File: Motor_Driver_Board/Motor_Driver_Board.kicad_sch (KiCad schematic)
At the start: 5 parts, among them J1 Conn_01x02_MountingPin, J2 Conn_01x04_MountingPin

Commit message: Shcematic and layout
Updated the schematic.
Updated the layout.
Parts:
- removed J1: Conn_01x02_MountingPin, Connector_PinHeader_2.54mm:PinHeader_1x02_P2.54mm_Vertical, symbol Connector_Generic_MountingPin:Conn_01x02_MountingPin
- removed J2: Conn_01x04_MountingPin, Connector_PinHeader_2.54mm:PinHeader_1x04_P2.54mm_Horizontal, symbol Connector_Generic_MountingPin:Conn_01x04_MountingPin
- added C2: 100u, Capacitor_THT:CP_Radial_D6.3mm_P2.50mm, symbol Device:C_Polarized
- added C3: 10u, Capacitor_SMD:C_1206_3216Metric, symbol Device:C
- added C4, C5, C6: 47u, Capacitor_SMD:C_1206_3216Metric, symbol Device:C
- added C7, C8, C9: 10n, Capacitor_SMD:C_0603_1608Metric, symbol Device:C
- added D1: SS34, Diode_SMD:D_SMA, symbol Diode:SS34
- added H1, H2, H3, H4: MH, MountingHole:MountingHole_3.2mm_M3, symbol Mechanical:MountingHole
- added J1: POWER, Connector_PinHeader_2.54mm:PinHeader_1x02_P2.54mm_Vertical, symbol Connector_Generic:Conn_01x02
- added J2: MOTOR, Connector_PinHeader_2.54mm:PinHeader_1x04_P2.54mm_Vertical, symbol Connector_Generic:Conn_01x04
- added J3: LCD, Connector_PinHeader_2.54mm:PinHeader_1x04_P2.54mm_Vertical, symbol Connector_Generic:Conn_01x04
- added L1: FXL1040-680-M, Inductor_SMD:L_Sunlord_MWSA1005S, symbol Device:L
- added R1, R10, R11, R2, R3, R4, R5, R6, R7, R8, R9: 10K, Resistor_SMD:R_0603_1608Metric, symbol Device:R
- added SW1: ENCODER, Rotary_Encoder:RotaryEncoder_Alps_EC11E-Switch_Vertical_H20mm_CircularMountingHoles, symbol Device:RotaryEncoder_Switch_MP
- added U1: XL1509-5.0, Package_SO:SOIC-8_3.9x4.9mm_P1.27mm, symbol Regulator_Switching:XL1509-5.0
- A1: value Pololu_Breakout_A4988 -> A4988
- C1: value C_Polarized 100uF -> 100u; footprint Capacitor_THT:CP_Axial_L18.0mm_D8.0mm_P25.00mm_Horizontal -> Capacitor_THT:CP_Radial_D6.3mm_P2.50mm
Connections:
- net GND: now also C2.2, C3.2, C4.2, C5.2, C6.2, C7.2, C8.2, C9.2, D1.2 (A), J1.2 (Pin_2), J3.4 (Pin_4), R7.2, R8.2, R9.2, SW1.C, SW1.S2, U1.5 (GND), U1.6 (GND), U1.7 (GND), U1.8 (GND); no longer A2.33 (AGND)
- net MS1: now reaches A1.10 (MS1), A2.6 (GPIO4)
- net MS1: now also R7.1
- net MS2: now reaches A1.11 (MS2), A2.5 (GPIO3)
- net MS2: now also R8.1
- net MS3: now reaches A1.12 (MS3), A2.4 (GPIO2)
- net MS3: now also R9.1
- net RST: now reaches A1.13 (~{RESET}), A1.14 (~{SLEEP})
- net DIR: now reaches A1.15 (STEP), A2.2 (GPIO1)
- net STEP: now reaches A1.16 (DIR), A2.1 (GPIO0)
- net at A2.40 (VBUS): no longer A1.2 (VDD)
- net B1: now reaches A1.3 (1B)
- net B1: now also J2.1 (Pin_1)
- net A1: now reaches A1.4 (1A)
- net A1: now also J2.2 (Pin_2)
- net A2: now reaches A1.5 (2A)
- net A2: now also J2.4 (Pin_4)
- net B2: now reaches A1.6 (2B)
- net B2: now also J2.3 (Pin_3)
- net VCC: now reaches A1.8 (VMOT), C1.1
- net VCC: now also C2.1, C3.1, J1.1 (Pin_1), U1.1 (VIN), U1.4 (~{EN})
- net SDA: now reaches A2.11 (GPIO8)
- net SDA: now also J3.1 (Pin_1), R10.2
- net SCL: now reaches A2.12 (GPIO9)
- net SCL: now also J3.2 (Pin_2), R11.2
- net ENC_CW: now reaches A2.15 (GPIO11)
- net ENC_CW: now also C7.1, R6.2
- net ENC_CC: now reaches A2.17 (GPIO13)
- net ENC_CC: now also C8.1, R4.2
- net ENC_SW: now reaches A2.20 (GPIO15)
- net ENC_SW: now also C9.1, R5.1
- net +3V3: now reaches A2.36 (3V3)
- net +3V3: now also J3.3 (Pin_3), R1.1, R10.1, R11.1, R2.1, R3.1
- net +5V: now reaches A2.39 (VSYS)
- net +5V: now also A1.2 (VDD), C4.1, C5.1, C6.1, L1.2, U1.3 (FB)
- new net: R2.2, R4.1, SW1.A
- new net: R1.2, R6.1, SW1.B
- new net: R3.2, R5.2, SW1.S1
- new net DC_OUT: D1.1 (K), L1.1, U1.2 (OUT)
- no-connect marks 29 -> 25
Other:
- note added: "DC-DC Regulator 5V/2A"
- note added: "ENCODER"
- note added: "I2C LCD"
- note added: "Motor"
- note added: "Power In 8-35V"
- note added: "RP PICO / RP2040"
- note removed: "Motor Input"
- note removed: "Motor Input Power 8-35V"
- moved on the sheet: A1, A2, C1

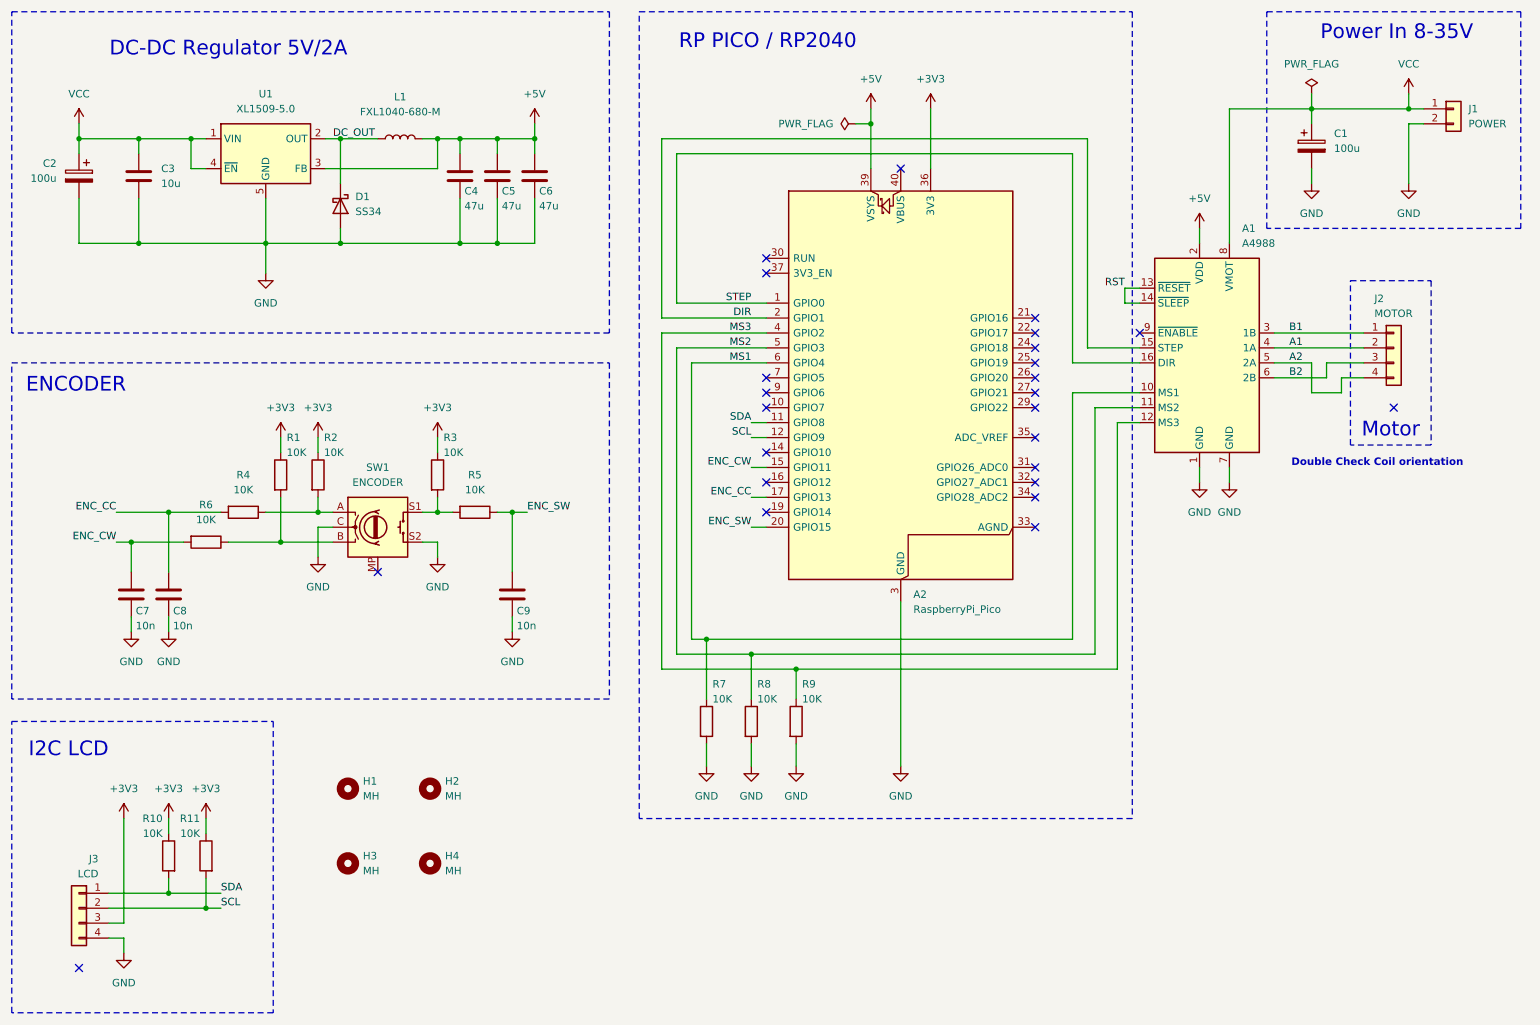
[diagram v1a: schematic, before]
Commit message: Switch to RP2040-Zero
Switched controller to RP2040-Zero to save space, schematic updated.
PCB layout in progress
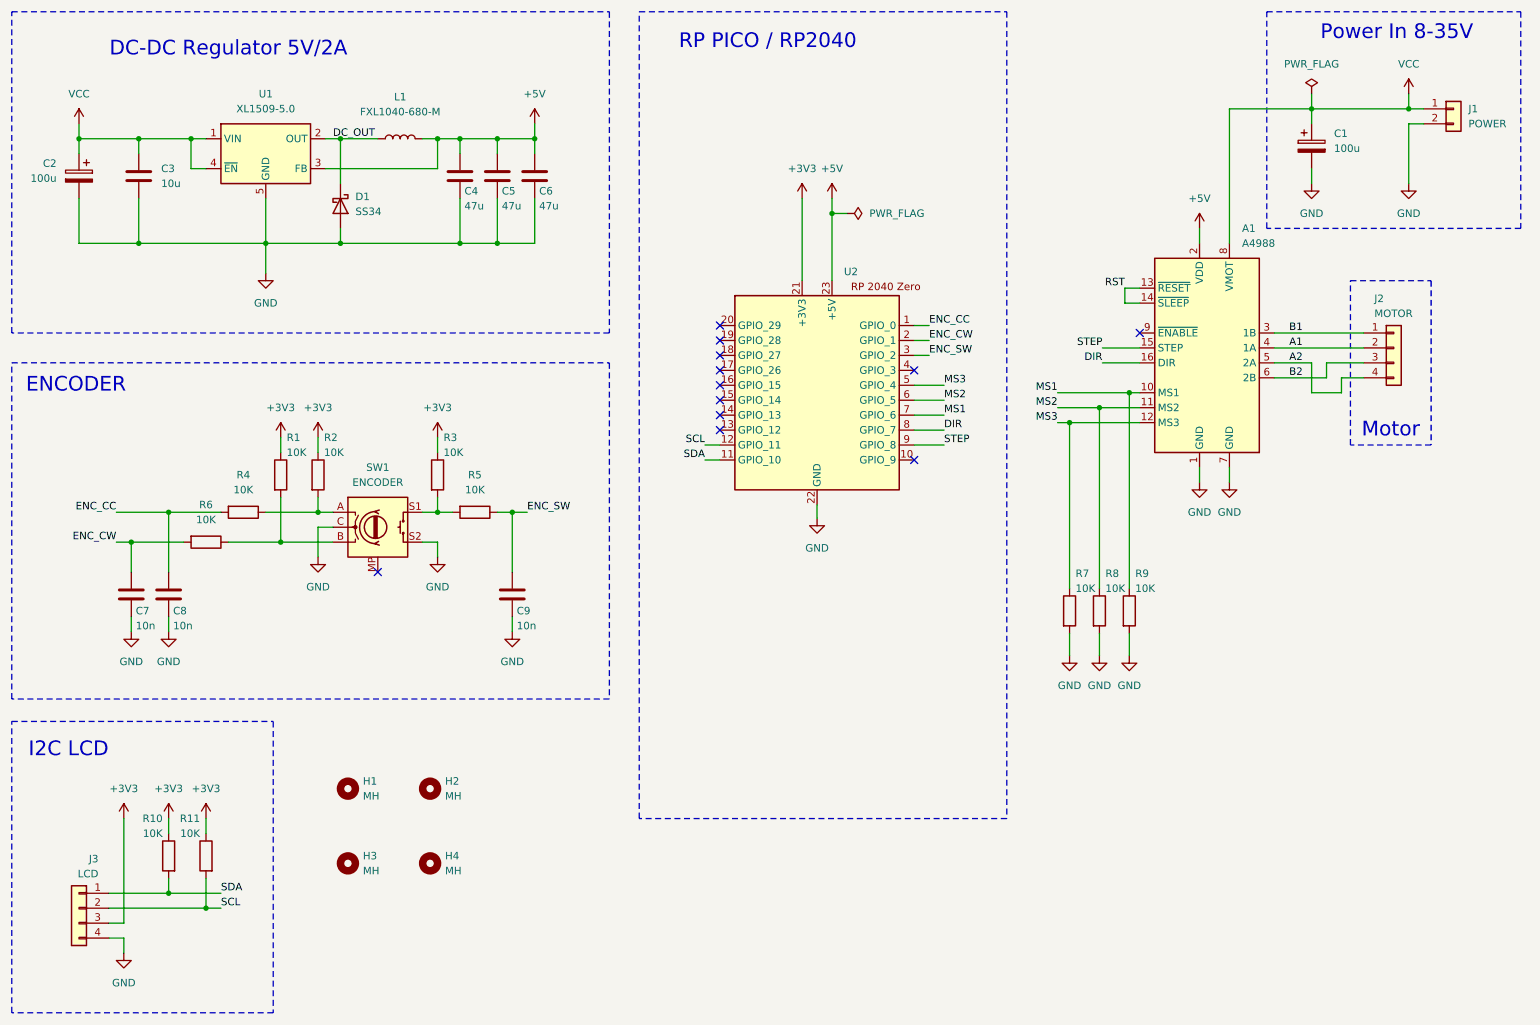
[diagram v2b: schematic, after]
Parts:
- removed A2: RaspberryPi_Pico, Module:RaspberryPi_Pico_Common_Unspecified, symbol MCU_Module:RaspberryPi_Pico
- added U2: (no value), RP2040Zero:MODULE_RP2040-ZERO, symbol RP2040_Zero:RP2040_Zero
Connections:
- net +3V3: now also U2.21 (+3V3)
- net +5V: now also U2.23 (+5V)
- net DIR: now also A1.16 (DIR), U2.8 (GPIO_7); no longer A1.15 (STEP)
- net ENC_CC: now also U2.1 (GPIO_0)
- net ENC_CW: now also U2.2 (GPIO_1)
- net ENC_SW: now also U2.3 (GPIO_2)
- net GND: now also U2.22 (GND)
- net MS1: now also R9.1, U2.7 (GPIO_6); no longer R7.1
- net MS2: now also U2.6 (GPIO_5)
- net MS3: now also R7.1, U2.5 (GPIO_4); no longer R9.1
- net SCL: now also U2.12 (GPIO_11)
- net SDA: now also U2.11 (GPIO_10)
- net STEP: now also A1.15 (STEP), U2.9 (GPIO_8); no longer A1.16 (DIR)
- no-connect marks 25 -> 12
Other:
- note removed: "Double Check Coil orientation"
- moved on the sheet: R7, R8, R9

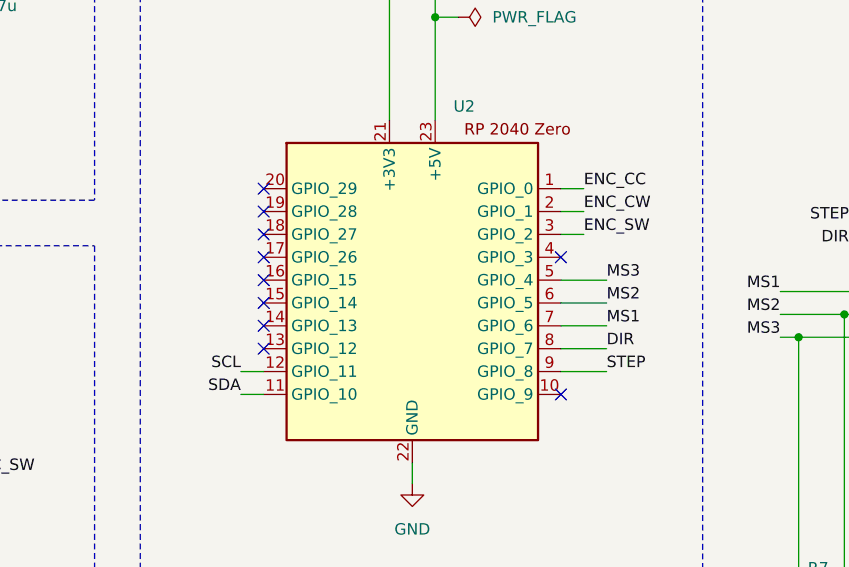
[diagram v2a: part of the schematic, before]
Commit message: Added RP2040-Zero Microcontroller
Switched previous Pi Pico to RP2040-Zero by Waveshare to reduce overall board size. Layout complete, via hatching still required
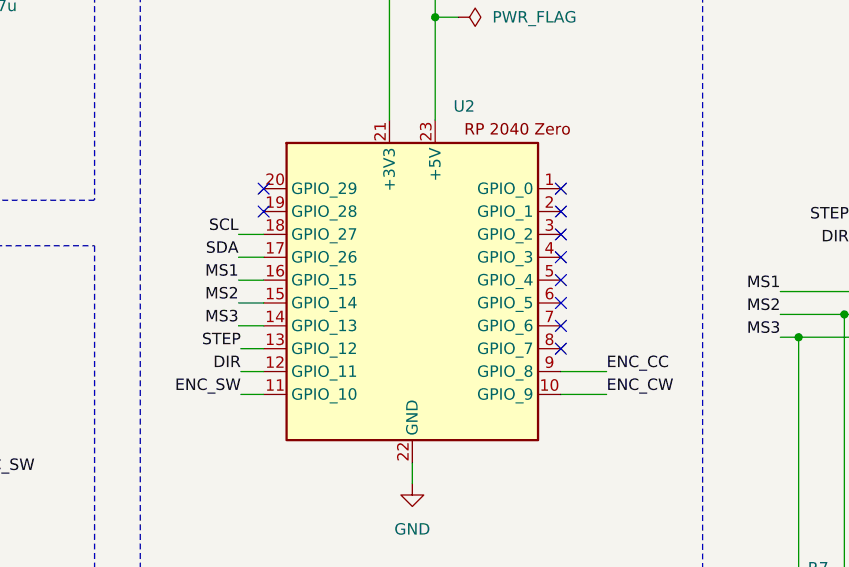
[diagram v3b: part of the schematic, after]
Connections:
- net DIR: now also U2.12 (GPIO_11); no longer U2.8 (GPIO_7)
- net ENC_CC: now also U2.9 (GPIO_8); no longer U2.1 (GPIO_0)
- net ENC_CW: now also U2.10 (GPIO_9); no longer U2.2 (GPIO_1)
- net ENC_SW: now also U2.11 (GPIO_10); no longer U2.3 (GPIO_2)
- net MS1: now also U2.16 (GPIO_15); no longer U2.7 (GPIO_6)
- net MS2: now also U2.15 (GPIO_14); no longer U2.6 (GPIO_5)
- net MS3: now also U2.14 (GPIO_13); no longer U2.5 (GPIO_4)
- net SCL: now also U2.18 (GPIO_27); no longer U2.12 (GPIO_11)
- net SDA: now also U2.17 (GPIO_26); no longer U2.11 (GPIO_10)
- net STEP: now also U2.13 (GPIO_12); no longer U2.9 (GPIO_8)
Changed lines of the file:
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@@
 	)
 	(no_connect
-		(at 140.716 91.44)
+		(at 173.736 76.2)
 	)
 	(no_connect
-		(at 140.716 93.98)
+		(at 173.736 93.98)
+	)
+	(no_connect
+		(at 173.736 91.44)
+	)
+	(no_connect
+		(at 140.716 78.74)
+	)
+	(no_connect
+		(at 140.716 76.2)
+	)
+	(no_connect
+		(at 173.736 83.82)
 	)
 	(no_connect
@@
 	)
 	(no_connect
-		(at 140.716 83.82)
+		(at 173.736 78.74)
 	)
 	(no_connect
-		(at 173.736 99.06)
+		(at 173.736 86.36)
 	)
 	(no_connect
-		(at 140.716 81.28)
+		(at 173.736 81.28)
 	)
 	(no_connect
-		(at 173.736 83.82)
-	)
-	(no_connect
-		(at 140.716 86.36)
-	)
-	(no_connect
-		(at 140.716 76.2)
-	)
-	(no_connect
-		(at 140.716 88.9)
-	)
-	(no_connect
-		(at 140.716 78.74)
+		(at 173.736 88.9)
 	)
 	(wire
@@
 	(wire
 		(pts
-			(xy 176.276 76.2) (xy 173.736 76.2)
-		)
-		(stroke
-			(width 0)
-			(type default)
-		)
-	)
-	(wire
-		(pts
 			(xy 55.88 175.26) (xy 53.34 175.26)
 		)
@@
 	(wire
 		(pts
-			(xy 173.736 88.9) (xy 178.816 88.9)
-		)
-		(stroke
-			(width 0)
-			(type default)
-		)
-	)
-	(wire
-		(pts
 			(xy 205.74 80.01) (xy 212.09 80.01)
 		)
@@
 	(wire
 		(pts
+			(xy 137.922 88.9) (xy 140.716 88.9)
+		)
+		(stroke
+			(width 0)
+			(type default)
+		)
+	)
+	(wire
+		(pts
 			(xy 92.71 107.95) (xy 90.17 107.95)
 		)
@@
 	(wire
 		(pts
-			(xy 176.276 78.74) (xy 173.736 78.74)
-		)
-		(stroke
-			(width 0)
-			(type default)
-		)
-	)
-	(wire
-		(pts
-			(xy 173.736 91.44) (xy 178.816 91.44)
-		)
-		(stroke
-			(width 0)
-			(type default)
-		)
-	)
-	(wire
-		(pts
 			(xy 210.312 87.63) (xy 210.312 120.904)
 		)
@@
 	(wire
 		(pts
-			(xy 176.276 81.28) (xy 173.736 81.28)
-		)
-		(stroke
-			(width 0)
-			(type default)
-		)
-	)
-	(wire
-		(pts
 			(xy 96.52 46.99) (xy 96.52 44.45)
 		)
@@
 	(wire
 		(pts
+			(xy 138.176 93.98) (xy 140.716 93.98)
+		)
+		(stroke
+			(width 0)
+			(type default)
+		)
+	)
+	(wire
+		(pts
 			(xy 92.71 49.53) (xy 92.71 44.45)
 		)
@@
 	(wire
 		(pts
-			(xy 173.736 93.98) (xy 178.816 93.98)
-		)
-		(stroke
-			(width 0)
-			(type default)
-		)
-	)
-	(wire
-		(pts
 			(xy 40.64 113.03) (xy 49.53 113.03)
 		)
@@
 	(wire
 		(pts
-			(xy 173.736 86.36) (xy 178.816 86.36)
-		)
-		(stroke
-			(width 0)
-			(type default)
-		)
-	)
-	(wire
-		(pts
 			(xy 40.64 125.73) (xy 40.64 128.27)
 		)
@@
 	(wire
 		(pts
+			(xy 137.922 81.28) (xy 140.716 81.28)
+		)
+		(stroke
+			(width 0)
+			(type default)
+		)
+	)
+	(wire
+		(pts
 			(xy 39.37 177.8) (xy 36.83 177.8)
 		)
@@
 	(wire
 		(pts
+			(xy 137.922 86.36) (xy 140.716 86.36)
+		)
+		(stroke
+			(width 0)
+			(type default)
+		)
+	)
+	(wire
+		(pts
 			(xy 72.39 105.41) (xy 72.39 107.95)
 		)
@@
 	(wire
 		(pts
+			(xy 173.736 99.06) (xy 178.816 99.06)
+		)
+		(stroke
+			(width 0)
+			(type default)
+		)
+	)
+	(wire
+		(pts
 			(xy 76.2 44.45) (xy 82.55 44.45)
 		)
@@
 	(wire
 		(pts
+			(xy 137.922 91.44) (xy 140.716 91.44)
+		)
+		(stroke
+			(width 0)
+			(type default)
+		)
+	)
+	(wire
+		(pts
 			(xy 205.74 82.55) (xy 212.09 82.55)
 		)
@@
 	(wire
 		(pts
+			(xy 137.922 83.82) (xy 140.716 83.82)
+		)
+		(stroke
+			(width 0)
+			(type default)
+		)
+	)
+	(wire
+		(pts
 			(xy 31.75 62.23) (xy 41.91 62.23)
 		)
@@
 	)
 	(label "ENC_CW"
-		(at 176.276 78.74 0)
+		(at 178.816 99.06 0)
 		(effects
 			(font
@@
 	)
 	(label "ENC_CC"
-		(at 176.276 76.2 0)
+		(at 178.816 96.52 0)
 		(effects
 			(font
@@
 	)
 	(label "SDA"
-		(at 138.176 99.06 180)
+		(at 137.922 83.82 180)
 		(effects
 			(font
@@
 	)
 	(label "MS3"
-		(at 178.816 86.36 0)
-		(effects
-			(font
-				(size 1.27 1.27)
-			)
-			(justify left bottom)
+		(at 137.922 91.44 180)
+		(effects
+			(font
+				(size 1.27 1.27)
+			)
+			(justify right bottom)
 		)
 	)
 	(label "DIR"
-		(at 178.816 93.98 0)
-		(effects
-			(font
-				(size 1.27 1.27)
-			)
-			(justify left bottom)
+		(at 138.176 96.52 180)
+		(effects
+			(font
+				(size 1.27 1.27)
+			)
+			(justify right bottom)
 		)
 	)
@@
 	)
 	(label "ENC_SW"
-		(at 176.276 81.28 0)
-		(effects
-			(font
-				(size 1.27 1.27)
-			)
-			(justify left bottom)
+		(at 138.176 99.06 180)
+		(effects
+			(font
+				(size 1.27 1.27)
+			)
+			(justify right bottom)
 		)
 	)
@@
 	)
 	(label "MS1"
-		(at 178.816 91.44 0)
-		(effects
-			(font
-				(size 1.27 1.27)
-			)
-			(justify left bottom)
+		(at 137.922 86.36 180)
+		(effects
+			(font
+				(size 1.27 1.27)
+			)
+			(justify right bottom)
 		)
 	)
@@
 	)
 	(label "MS2"
-		(at 178.816 88.9 0)
-		(effects
-			(font
-				(size 1.27 1.27)
-			)
-			(justify left bottom)
+		(at 137.922 88.9 180)
+		(effects
+			(font
+				(size 1.27 1.27)
+			)
+			(justify right bottom)
 		)
 	)
 	(label "SCL"
-		(at 138.176 96.52 180)
+		(at 137.922 81.28 180)
 		(effects
 			(font
@@
 	)
 	(label "STEP"
-		(at 178.816 96.52 0)
-		(effects
-			(font
-				(size 1.27 1.27)
-			)
-			(justify left bottom)
-		)
-	)
+		(at 138.176 93.98 180)
+		(effects
+			(font
+				(size 1.27 1.27)
+			)
+			(justify right bottom)
+		)
+	)
